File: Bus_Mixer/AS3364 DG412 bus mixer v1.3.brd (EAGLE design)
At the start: 83.8 x 42.9 mm, 122 parts, among them IC1 PCA9539PW, IC10 DG412-J, IC11 DG412-J, IC2 TL074JT, IC3 TL072JT, IC4 TL074JT, IC5 TL072JT, IC6 TL072JT, IC8 DG412-J, IC9 DG412-J

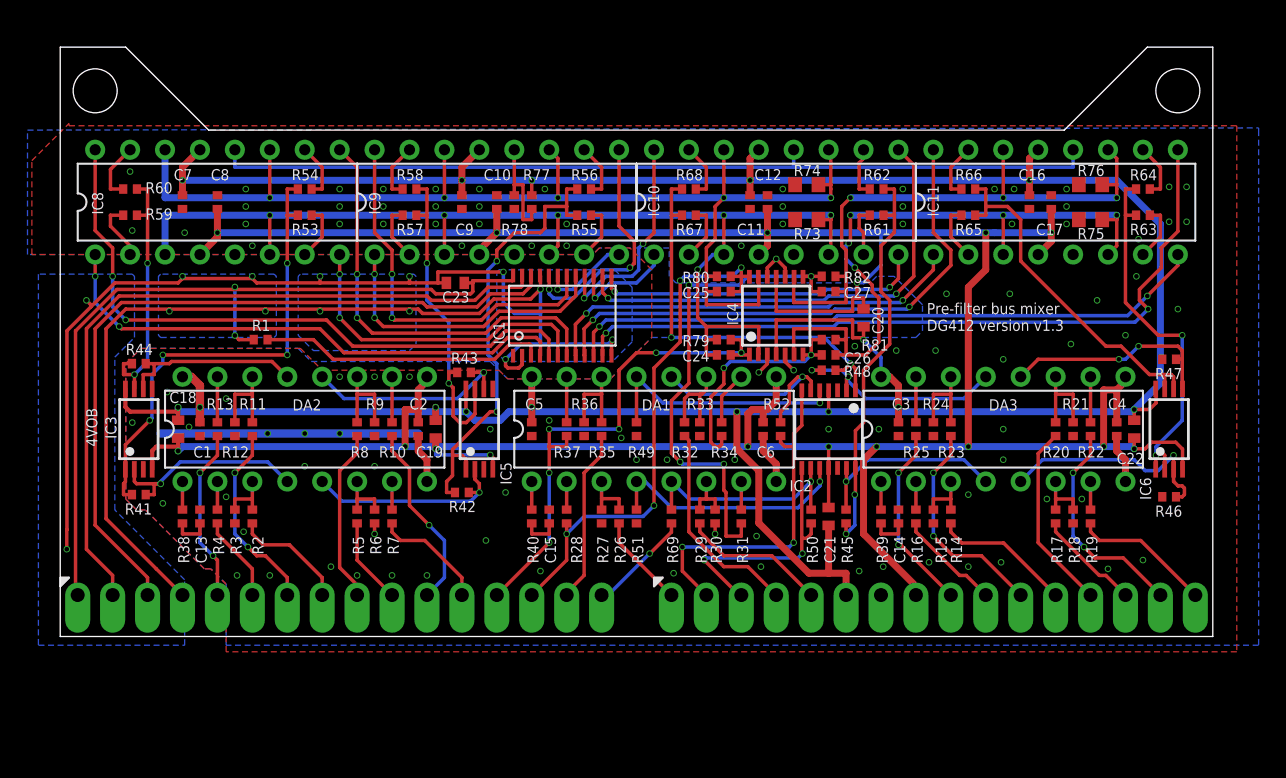
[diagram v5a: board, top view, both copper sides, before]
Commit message: Added screw holes
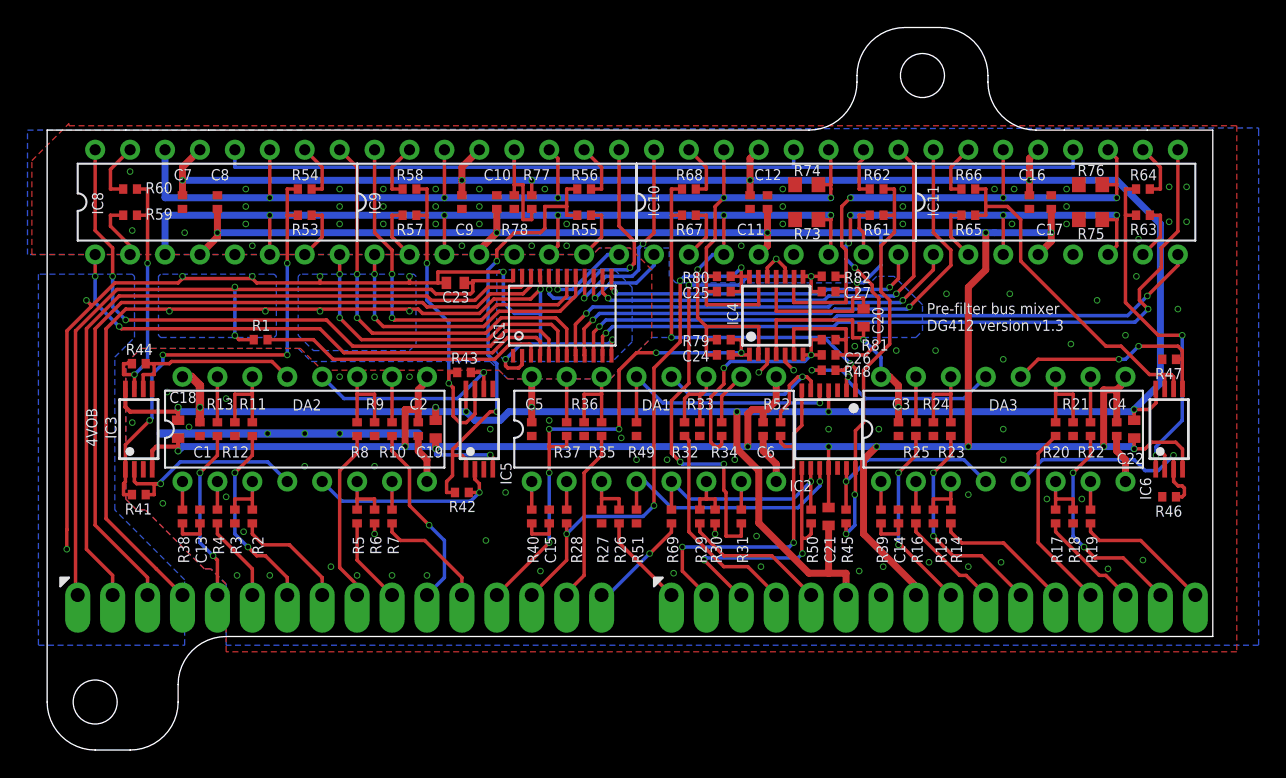
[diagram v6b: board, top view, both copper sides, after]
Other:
- board size 83.8 x 42.9 mm -> 84.8 x 52.5 mm
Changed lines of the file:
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@@
 <setting verticaltext="up"/>
 </settings>
-<grid distance="12.5" unitdist="mil" unit="mil" style="lines" multiple="1" display="yes" altdistance="5" altunitdist="mil" altunit="mil"/>
+<grid distance="6.25" unitdist="mil" unit="mm" style="lines" multiple="1" display="yes" altdistance="5" altunitdist="mil" altunit="mil"/>
 <layers>
 <layer number="1" name="Top" color="4" fill="1" visible="yes" active="yes"/>
@@
 <layer number="43" name="vRestrict" color="2" fill="10" visible="no" active="yes"/>
 <layer number="44" name="Drills" color="7" fill="1" visible="no" active="yes"/>
-<layer number="45" name="Holes" color="7" fill="1" visible="no" active="yes"/>
+<layer number="45" name="Holes" color="7" fill="1" visible="yes" active="yes"/>
 <layer number="46" name="Milling" color="3" fill="1" visible="no" active="yes"/>
 <layer number="47" name="Measures" color="7" fill="1" visible="no" active="yes"/>
@@
 <board>
 <plain>
-<wire x1="0" y1="0" x2="83.82" y2="0" width="0" layer="20"/>
-<wire x1="83.82" y1="0" x2="83.82" y2="42.8625" width="0" layer="20"/>
-<wire x1="83.82" y1="42.8625" x2="79.0575" y2="42.8625" width="0" layer="20"/>
-<wire x1="79.0575" y1="42.8625" x2="73.025" y2="36.83" width="0" layer="20"/>
-<wire x1="73.025" y1="36.83" x2="10.795" y2="36.83" width="0" layer="20"/>
-<wire x1="10.795" y1="36.83" x2="4.7625" y2="42.8625" width="0" layer="20"/>
-<wire x1="4.7625" y1="42.8625" x2="0" y2="42.8625" width="0" layer="20"/>
-<wire x1="0" y1="42.8625" x2="0" y2="0" width="0" layer="20"/>
+<wire x1="2.54" y1="-8.255" x2="5.08" y2="-8.255" width="0" layer="20"/>
+<wire x1="83.82" y1="0" x2="83.82" y2="36.83" width="0" layer="20"/>
+<wire x1="83.82" y1="36.83" x2="79.0575" y2="36.83" width="0" layer="20"/>
+<wire x1="79.0575" y1="36.83" x2="73.025" y2="36.83" width="0" layer="20"/>
+<wire x1="73.025" y1="36.83" x2="70.96125" y2="36.83" width="0" layer="20"/>
+<wire x1="54.45125" y1="36.83" x2="10.795" y2="36.83" width="0" layer="20"/>
+<wire x1="10.795" y1="36.83" x2="4.7625" y2="36.83" width="0" layer="20"/>
+<wire x1="4.7625" y1="36.83" x2="-0.9525" y2="36.83" width="0" layer="20"/>
+<wire x1="-0.9525" y1="36.83" x2="-0.9525" y2="-4.7625" width="0" layer="20"/>
 <text x="63.02375" y="22.225" size="0.8128" layer="25" font="vector">Pre-filter bus mixer
 DG412 version v1.3</text>
@@
 <text x="31.115" y="4.60375" size="1.27" layer="26" font="vector" rot="MR90">SUM A</text>
 <text x="38.735" y="4.60375" size="1.27" layer="26" font="vector" rot="MR90">CHAIN</text>
-<hole x="2.54" y="39.6875" drill="3.2"/>
 <circle x="2.54" y="39.6875" radius="3" width="0.254" layer="49"/>
-<hole x="81.28" y="39.6875" drill="3.2"/>
+<hole x="62.70625" y="40.79875" drill="3.2"/>
 <circle x="81.28" y="39.6875" radius="3" width="0.254" layer="49"/>
+<hole x="2.54" y="-4.7625" drill="3.2"/>
+<circle x="2.54" y="-4.7625" radius="3" width="0.127" layer="51"/>
+<wire x1="2.54" y1="-8.255" x2="-0.9525" y2="-4.7625" width="0" layer="20" curve="-90"/>
+<wire x1="8.5725" y1="-4.7625" x2="5.08" y2="-8.255" width="0" layer="20" curve="-90"/>
+<wire x1="8.5725" y1="-3.4925" x2="12.065" y2="0" width="0" layer="20" curve="-90"/>
+<wire x1="8.5725" y1="-3.4925" x2="8.5725" y2="-4.7625" width="0" layer="20"/>
+<wire x1="12.065" y1="0" x2="83.82" y2="0" width="0" layer="20"/>
+<circle x="62.70625" y="40.79875" radius="3" width="0.127" layer="51"/>
+<wire x1="63.97625" y1="44.29125" x2="61.43625" y2="44.29125" width="0" layer="20"/>
+<wire x1="63.97625" y1="44.29125" x2="67.46875" y2="40.79875" width="0" layer="20" curve="-90"/>
+<wire x1="57.94375" y1="40.79875" x2="61.43625" y2="44.29125" width="0" layer="20" curve="-90"/>
+<wire x1="57.94375" y1="40.3225" x2="54.45125" y2="36.83" width="0" layer="20" curve="-90"/>
+<wire x1="70.96125" y1="36.83" x2="67.46875" y2="40.3225" width="0" layer="20" curve="-90"/>
+<wire x1="67.46875" y1="40.79875" x2="67.46875" y2="40.3225" width="0" layer="20"/>
+<wire x1="57.94375" y1="40.79875" x2="57.94375" y2="40.3225" width="0" layer="20"/>
 </plain>
 <attributes>

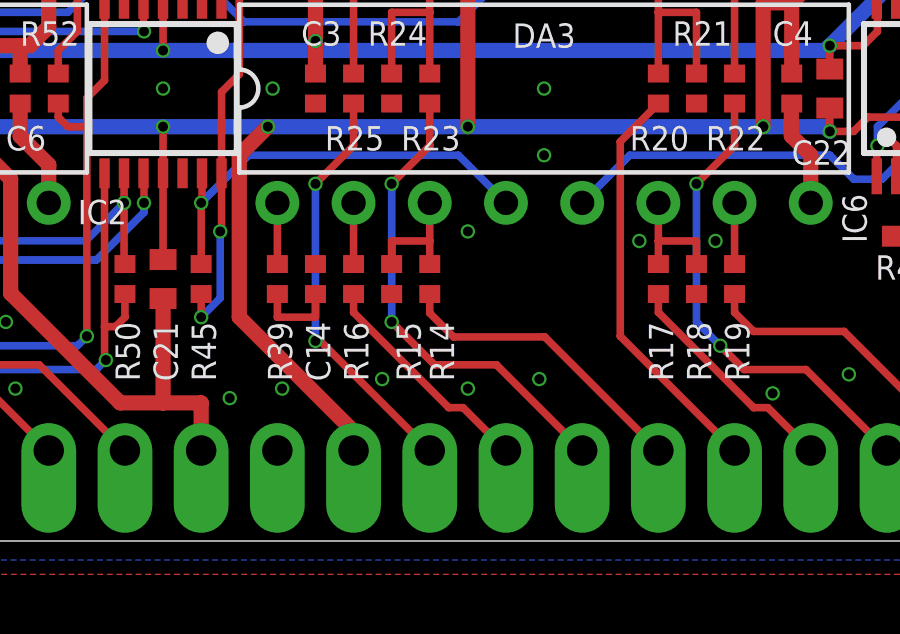
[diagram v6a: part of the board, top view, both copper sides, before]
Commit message: Added increase-gain resistor to noise input
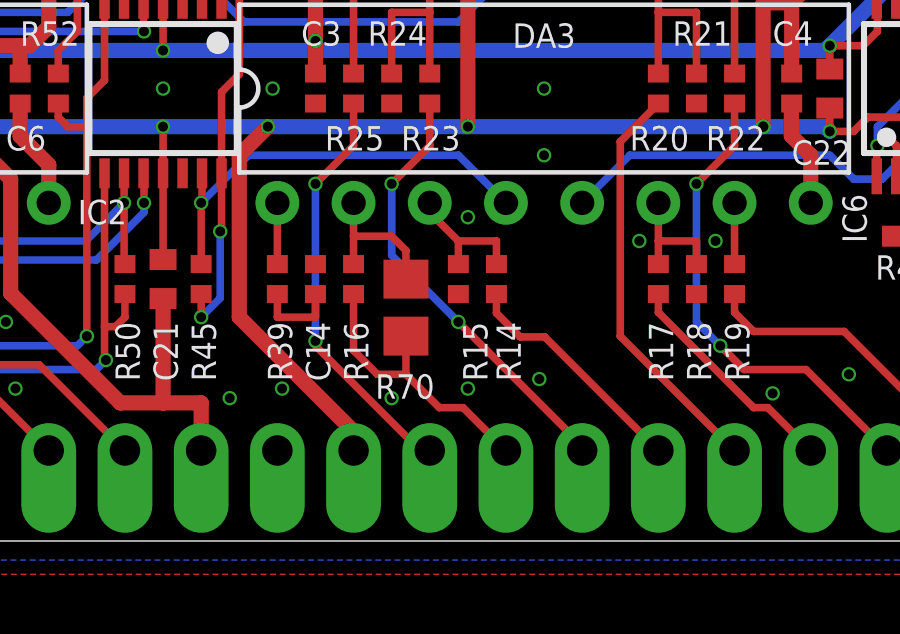
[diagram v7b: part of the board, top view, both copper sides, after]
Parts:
- added R70: DNM, rcl:R0805
- moved R14 2.22 mm to (67.0, 8.73)
- moved R15 2.22 mm to (65.7, 8.73)
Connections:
- net IN6: now also R70.1
- net SUM6: now also R70.2
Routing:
- net SUM6: track 2.04 -> 4.94 mm
- net CV6: track 10.2 -> 7.93 mm
- net IN6: track 7.60 -> 9.61 mm
- net CV5: track 15.9 -> 14.8 mm

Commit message: Switched to female pin headers
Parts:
- U$2, U$3: value MA16-1JP-ANGLED -> MA16-1JP-FEMALE
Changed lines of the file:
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@@
 <attribute name="VALUE" x="42.545" y="9.36625" size="1.27" layer="27" rot="R270"/>
 </element>
-<element name="U$2" library="joakim" package="SIP-PIN16-1J" value="MA16-1JP-ANGLED" x="63.5" y="3.01625" smashed="yes">
+<element name="U$2" library="joakim" package="SIP-PIN16-1J" value="MA16-1JP-FEMALE" x="63.5" y="3.01625" smashed="yes">
 <attribute name="VALUE" x="43.18" y="-1.17475" size="1.27" layer="27" ratio="10"/>
 </element>
-<element name="U$3" library="joakim" package="SIP-PIN16-1J" value="MA16-1JP-ANGLED" x="20.32" y="3.01625" smashed="yes">
+<element name="U$3" library="joakim" package="SIP-PIN16-1J" value="MA16-1JP-FEMALE" x="20.32" y="3.01625" smashed="yes">
 <attribute name="VALUE" x="0" y="-1.17475" size="1.27" layer="27" ratio="10"/>
 </element>
